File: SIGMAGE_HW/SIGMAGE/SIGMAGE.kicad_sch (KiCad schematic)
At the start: 0 parts

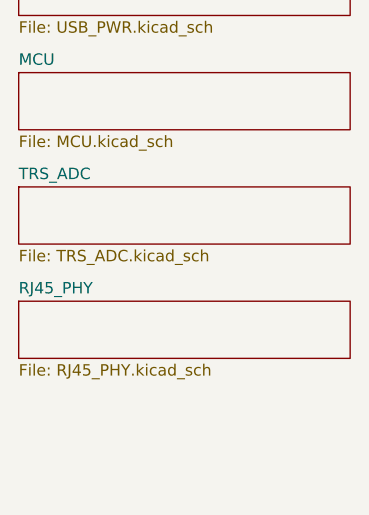
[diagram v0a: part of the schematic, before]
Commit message: Adding a view DAC's
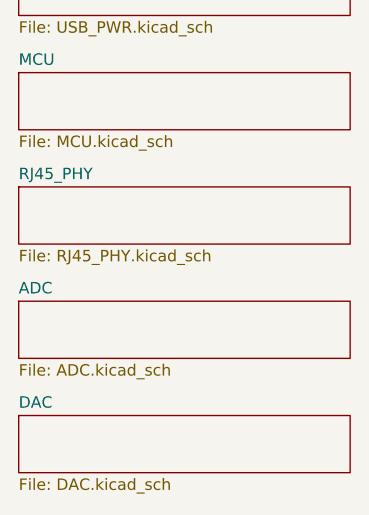
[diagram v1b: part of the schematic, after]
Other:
- removed sheet TRS_ADC
- added sheet ADC (ADC.kicad_sch)
- added sheet DAC (DAC.kicad_sch)
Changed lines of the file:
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@@
+	)
+	(sheet
+		(at 17.78 57.15)
+		(size 36.83 6.35)
+		(exclude_from_sim no)
+		(in_bom yes)
+		(on_board yes)
+		(dnp no)
+		(fields_autoplaced yes)
+		(stroke
+			(width 0.1524)
+			(type solid)
+		)
+		(fill
+			(color 0 0 0 0)
+		)
+		(property "Sheetname" "ADC"
+			(at 17.78 56.4384 0)
+			(show_name no)
+			(do_not_autoplace no)
+			(effects
+				(font
+					(size 1.27 1.27)
+				)
+				(justify left bottom)
+			)
+		)
+		(property "Sheetfile" "ADC.kicad_sch"
+			(at 17.78 64.0846 0)
+			(show_name no)
+			(do_not_autoplace no)
+			(effects
+				(font
+					(size 1.27 1.27)
+				)
+				(justify left top)
+			)
+		)
+		(instances
+			(project "SIGMAGE"
+				(path "/6fbe3371-b6a3-4e28-aef4-4e5865f4674e"
+					(page "3")
+				)
+			)
+		)
 	)
 	(sheet
@@
 			(color 0 0 0 0)
 		)
-		(property "Sheetname" "TRS_ADC"
+		(property "Sheetname" "RJ45_PHY"
 			(at 17.78 43.7384 0)
 			(show_name no)
@@
 			)
 		)
-		(property "Sheetfile" "TRS_ADC.kicad_sch"
+		(property "Sheetfile" "RJ45_PHY.kicad_sch"
 			(at 17.78 51.3846 0)
 			(show_name no)
@@
 	)
 	(sheet
-		(at 17.78 57.15)
+		(at 17.78 69.85)
 		(size 36.83 6.35)
 		(exclude_from_sim no)
@@
 			(color 0 0 0 0)
 		)
-		(property "Sheetname" "RJ45_PHY"
-			(at 17.78 56.4384 0)
+		(property "Sheetname" "DAC"
+			(at 17.78 69.1384 0)
 			(show_name no)
 			(do_not_autoplace no)
@@
 			)
 		)
-		(property "Sheetfile" "RJ45_PHY.kicad_sch"
-			(at 17.78 64.0846 0)
+		(property "Sheetfile" "DAC.kicad_sch"
+			(at 17.78 76.7846 0)
 			(show_name no)
 			(do_not_autoplace no)
@@
 			(project "SIGMAGE"
 				(path "/6fbe3371-b6a3-4e28-aef4-4e5865f4674e"
-					(page "5")
+					(page "6")
 				)
 			)

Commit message: some schematic adjustments
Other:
- removed sheet MCU
- removed sheet RJ45_PHY
- added sheet FPGA (FPGA.kicad_sch)
- added sheet PWR (PWR.kicad_sch)
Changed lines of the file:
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@@
 	(paper "A4")
 	(sheet
-		(at 17.78 31.75)
-		(size 36.83 6.35)
-		(exclude_from_sim no)
-		(in_bom yes)
-		(on_board yes)
-		(dnp no)
-		(fields_autoplaced yes)
-		(stroke
-			(width 0.1524)
-			(type solid)
-		)
-		(fill
-			(color 0 0 0 0)
-		)
-		(property "Sheetname" "MCU"
-			(at 17.78 31.0384 0)
-			(show_name no)
-			(do_not_autoplace no)
-			(effects
-				(font
-					(size 1.27 1.27)
-				)
-				(justify left bottom)
-			)
-		)
-		(property "Sheetfile" "MCU.kicad_sch"
-			(at 17.78 38.6846 0)
+		(at 62.23 19.05)
+		(size 36.83 6.35)
+		(exclude_from_sim no)
+		(in_bom yes)
+		(on_board yes)
+		(dnp no)
+		(fields_autoplaced yes)
+		(stroke
+			(width 0.1524)
+			(type solid)
+		)
+		(fill
+			(color 0 0 0 0)
+		)
+		(property "Sheetname" "USB_PWR"
+			(at 62.23 18.3384 0)
+			(show_name no)
+			(do_not_autoplace no)
+			(effects
+				(font
+					(size 1.27 1.27)
+				)
+				(justify left bottom)
+			)
+		)
+		(property "Sheetfile" "USB_PWR.kicad_sch"
+			(at 62.23 25.9846 0)
+			(show_name no)
+			(do_not_autoplace no)
+			(effects
+				(font
+					(size 1.27 1.27)
+				)
+				(justify left top)
+			)
+		)
+		(instances
+			(project "SIGMAGE"
+				(path "/6fbe3371-b6a3-4e28-aef4-4e5865f4674e"
+					(page "2")
+				)
+			)
+		)
+	)
+	(sheet
+		(at 19.05 31.75)
+		(size 36.83 6.35)
+		(exclude_from_sim no)
+		(in_bom yes)
+		(on_board yes)
+		(dnp no)
+		(fields_autoplaced yes)
+		(stroke
+			(width 0.1524)
+			(type solid)
+		)
+		(fill
+			(color 0 0 0 0)
+		)
+		(property "Sheetname" "FPGA"
+			(at 19.05 31.0384 0)
+			(show_name no)
+			(do_not_autoplace no)
+			(effects
+				(font
+					(size 1.27 1.27)
+				)
+				(justify left bottom)
+			)
+		)
+		(property "Sheetfile" "FPGA.kicad_sch"
+			(at 19.05 38.6846 0)
 			(show_name no)
 			(do_not_autoplace no)
@@
 	)
 	(sheet
-		(at 17.78 19.05)
-		(size 36.83 6.35)
-		(exclude_from_sim no)
-		(in_bom yes)
-		(on_board yes)
-		(dnp no)
-		(fields_autoplaced yes)
-		(stroke
-			(width 0.1524)
-			(type solid)
-		)
-		(fill
-			(color 0 0 0 0)
-		)
-		(property "Sheetname" "USB_PWR"
-			(at 17.78 18.3384 0)
-			(show_name no)
-			(do_not_autoplace no)
-			(effects
-				(font
-					(size 1.27 1.27)
-				)
-				(justify left bottom)
-			)
-		)
-		(property "Sheetfile" "USB_PWR.kicad_sch"
-			(at 17.78 25.9846 0)
-			(show_name no)
-			(do_not_autoplace no)
-			(effects
-				(font
-					(size 1.27 1.27)
-				)
-				(justify left top)
-			)
-		)
-		(instances
-			(project "SIGMAGE"
-				(path "/6fbe3371-b6a3-4e28-aef4-4e5865f4674e"
-					(page "2")
-				)
-			)
-		)
-	)
-	(sheet
-		(at 17.78 57.15)
+		(at 19.05 19.05)
+		(size 36.83 6.35)
+		(exclude_from_sim no)
+		(in_bom yes)
+		(on_board yes)
+		(dnp no)
+		(fields_autoplaced yes)
+		(stroke
+			(width 0.1524)
+			(type solid)
+		)
+		(fill
+			(color 0 0 0 0)
+		)
+		(property "Sheetname" "PWR"
+			(at 19.05 18.3384 0)
+			(show_name no)
+			(do_not_autoplace no)
+			(effects
+				(font
+					(size 1.27 1.27)
+				)
+				(justify left bottom)
+			)
+		)
+		(property "Sheetfile" "PWR.kicad_sch"
+			(at 19.05 25.9846 0)
+			(show_name no)
+			(do_not_autoplace no)
+			(effects
+				(font
+					(size 1.27 1.27)
+				)
+				(justify left top)
+			)
+		)
+		(instances
+			(project "SIGMAGE"
+				(path "/6fbe3371-b6a3-4e28-aef4-4e5865f4674e"
+					(page "5")
+				)
+			)
+		)
+	)
+	(sheet
+		(at 19.05 44.45)
 		(size 36.83 6.35)
 		(exclude_from_sim no)
@@
 		)
 		(property "Sheetname" "ADC"
-			(at 17.78 56.4384 0)
+			(at 19.05 43.7384 0)
 			(show_name no)
 			(do_not_autoplace no)
@@
 		)
 		(property "Sheetfile" "ADC.kicad_sch"
-			(at 17.78 64.0846 0)
+			(at 19.05 51.3846 0)
 			(show_name no)
 			(do_not_autoplace no)
@@
 	)
 	(sheet
-		(at 17.78 44.45)
-		(size 36.83 6.35)
-		(exclude_from_sim no)
-		(in_bom yes)
-		(on_board yes)
-		(dnp no)
-		(fields_autoplaced yes)
-		(stroke
-			(width 0.1524)
-			(type solid)
-		)
-		(fill
-			(color 0 0 0 0)
-		)
-		(property "Sheetname" "RJ45_PHY"
-			(at 17.78 43.7384 0)
-			(show_name no)
-			(do_not_autoplace no)
-			(effects
-				(font
-					(size 1.27 1.27)
-				)
-				(justify left bottom)
-			)
-		)
-		(property "Sheetfile" "RJ45_PHY.kicad_sch"
-			(at 17.78 51.3846 0)
-			(show_name no)
-			(do_not_autoplace no)
-			(effects
-				(font
-					(size 1.27 1.27)
-				)
-				(justify left top)
-			)
-		)
-		(instances
-			(project "SIGMAGE"
-				(path "/6fbe3371-b6a3-4e28-aef4-4e5865f4674e"
-					(page "5")
-				)
-			)
-		)
-	)
-	(sheet
-		(at 17.78 69.85)
+		(at 19.05 57.15)
 		(size 36.83 6.35)
 		(exclude_from_sim no)
@@
 		)
 		(property "Sheetname" "DAC"
-			(at 17.78 69.1384 0)
+			(at 19.05 56.4384 0)
 			(show_name no)
 			(do_not_autoplace no)
@@
 		)
 		(property "Sheetfile" "DAC.kicad_sch"
-			(at 17.78 76.7846 0)
-			(show_name no)
-			(do_not_autoplace no)
+			(at 19.05 64.0846 0)
+			(show_name no)
+			(do_not_autoplace no)

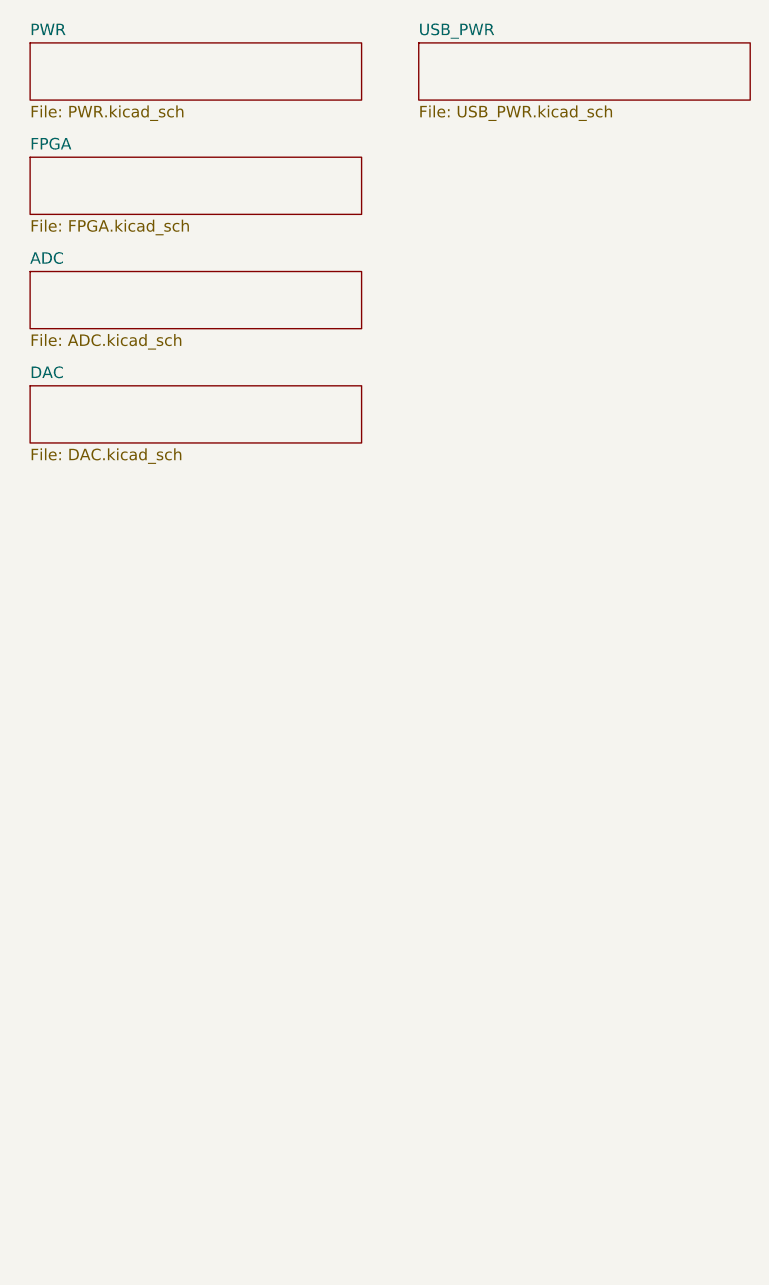
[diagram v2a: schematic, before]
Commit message: some USB interface
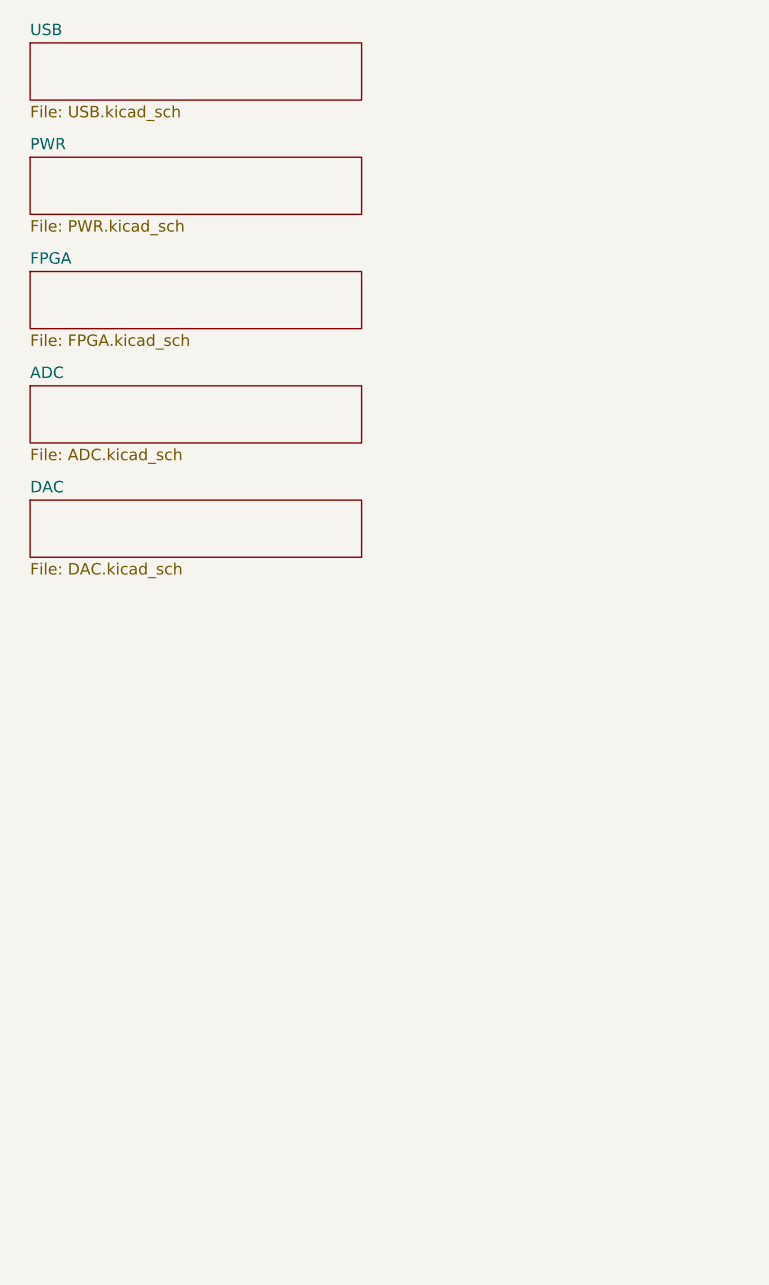
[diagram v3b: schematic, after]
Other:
- removed sheet USB_PWR
- added sheet USB (USB.kicad_sch)
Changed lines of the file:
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@@
 	(paper "A4")
 	(sheet
-		(at 62.23 19.05)
-		(size 36.83 6.35)
-		(exclude_from_sim no)
-		(in_bom yes)
-		(on_board yes)
-		(dnp no)
-		(fields_autoplaced yes)
-		(stroke
-			(width 0.1524)
-			(type solid)
-		)
-		(fill
-			(color 0 0 0 0)
-		)
-		(property "Sheetname" "USB_PWR"
-			(at 62.23 18.3384 0)
-			(show_name no)
-			(do_not_autoplace no)
-			(effects
-				(font
-					(size 1.27 1.27)
-				)
-				(justify left bottom)
-			)
-		)
-		(property "Sheetfile" "USB_PWR.kicad_sch"
-			(at 62.23 25.9846 0)
-			(show_name no)
-			(do_not_autoplace no)
-			(effects
-				(font
-					(size 1.27 1.27)
-				)
-				(justify left top)
-			)
-		)
-		(instances
-			(project "SIGMAGE"
-				(path "/6fbe3371-b6a3-4e28-aef4-4e5865f4674e"
-					(page "2")
+		(at 19.05 44.45)
+		(size 36.83 6.35)
+		(exclude_from_sim no)
+		(in_bom yes)
+		(on_board yes)
+		(dnp no)
+		(fields_autoplaced yes)
+		(stroke
+			(width 0.1524)
+			(type solid)
+		)
+		(fill
+			(color 0 0 0 0)
+		)
+		(property "Sheetname" "FPGA"
+			(at 19.05 43.7384 0)
+			(show_name no)
+			(do_not_autoplace no)
+			(effects
+				(font
+					(size 1.27 1.27)
+				)
+				(justify left bottom)
+			)
+		)
+		(property "Sheetfile" "FPGA.kicad_sch"
+			(at 19.05 51.3846 0)
+			(show_name no)
+			(do_not_autoplace no)
+			(effects
+				(font
+					(size 1.27 1.27)
+				)
+				(justify left top)
+			)
+		)
+		(instances
+			(project "SIGMAGE"
+				(path "/6fbe3371-b6a3-4e28-aef4-4e5865f4674e"
+					(page "4")
 				)
 			)
@@
 			(color 0 0 0 0)
 		)
-		(property "Sheetname" "FPGA"
+		(property "Sheetname" "PWR"
 			(at 19.05 31.0384 0)
 			(show_name no)
@@
 			)
 		)
-		(property "Sheetfile" "FPGA.kicad_sch"
+		(property "Sheetfile" "PWR.kicad_sch"
 			(at 19.05 38.6846 0)
 			(show_name no)
@@
 			(project "SIGMAGE"
 				(path "/6fbe3371-b6a3-4e28-aef4-4e5865f4674e"
-					(page "4")
+					(page "5")
+				)
+			)
+		)
+	)
+	(sheet
+		(at 19.05 57.15)
+		(size 36.83 6.35)
+		(exclude_from_sim no)
+		(in_bom yes)
+		(on_board yes)
+		(dnp no)
+		(fields_autoplaced yes)
+		(stroke
+			(width 0.1524)
+			(type solid)
+		)
+		(fill
+			(color 0 0 0 0)
+		)
+		(property "Sheetname" "ADC"
+			(at 19.05 56.4384 0)
+			(show_name no)
+			(do_not_autoplace no)
+			(effects
+				(font
+					(size 1.27 1.27)
+				)
+				(justify left bottom)
+			)
+		)
+		(property "Sheetfile" "ADC.kicad_sch"
+			(at 19.05 64.0846 0)
+			(show_name no)
+			(do_not_autoplace no)
+			(effects
+				(font
+					(size 1.27 1.27)
+				)
+				(justify left top)
+			)
+		)
+		(instances
+			(project "SIGMAGE"
+				(path "/6fbe3371-b6a3-4e28-aef4-4e5865f4674e"
+					(page "3")
 				)
 			)
@@
 			(color 0 0 0 0)
 		)
-		(property "Sheetname" "PWR"
+		(property "Sheetname" "USB"
 			(at 19.05 18.3384 0)
 			(show_name no)
@@
 			)
 		)
-		(property "Sheetfile" "PWR.kicad_sch"
+		(property "Sheetfile" "USB.kicad_sch"
 			(at 19.05 25.9846 0)
 			(show_name no)
@@
 			(project "SIGMAGE"
 				(path "/6fbe3371-b6a3-4e28-aef4-4e5865f4674e"
-					(page "5")
-				)
-			)
-		)
-	)
-	(sheet
-		(at 19.05 44.45)
-		(size 36.83 6.35)
-		(exclude_from_sim no)
-		(in_bom yes)
-		(on_board yes)
-		(dnp no)
-		(fields_autoplaced yes)
-		(stroke
-			(width 0.1524)
-			(type solid)
-		)
-		(fill
-			(color 0 0 0 0)
-		)
-		(property "Sheetname" "ADC"
-			(at 19.05 43.7384 0)
-			(show_name no)
-			(do_not_autoplace no)
-			(effects
-				(font
-					(size 1.27 1.27)
-				)
-				(justify left bottom)
-			)
-		)
-		(property "Sheetfile" "ADC.kicad_sch"
-			(at 19.05 51.3846 0)
-			(show_name no)
-			(do_not_autoplace no)
-			(effects
-				(font
-					(size 1.27 1.27)
-				)
-				(justify left top)
-			)
-		)
-		(instances
-			(project "SIGMAGE"
-				(path "/6fbe3371-b6a3-4e28-aef4-4e5865f4674e"
-					(page "3")
-				)
-			)
-		)
-	)
-	(sheet
-		(at 19.05 57.15)
+					(page "7")
+				)
+			)
+		)
+	)
+	(sheet
+		(at 19.05 69.85)
 		(size 36.83 6.35)
 		(exclude_from_sim no)
@@
 		)
 		(property "Sheetname" "DAC"
-			(at 19.05 56.4384 0)
+			(at 19.05 69.1384 0)
 			(show_name no)
 			(do_not_autoplace no)
@@
 		)
 		(property "Sheetfile" "DAC.kicad_sch"
-			(at 19.05 64.0846 0)
-			(show_name no)
-			(do_not_autoplace no)
+			(at 19.05 76.7846 0)
+			(show_name no)
+			(do_not_autoplace no)

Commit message: some changes
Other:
- added sheet ENC (ENC.kicad_sch)
- added sheet MCU (MCU.kicad_sch)
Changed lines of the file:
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@@
 	(paper "A4")
 	(sheet
-		(at 19.05 44.45)
+		(at 19.05 57.15)
 		(size 36.83 6.35)
 		(exclude_from_sim no)
@@
 		)
 		(property "Sheetname" "FPGA"
-			(at 19.05 43.7384 0)
+			(at 19.05 56.4384 0)
 			(show_name no)
 			(do_not_autoplace no)
@@
 		)
 		(property "Sheetfile" "FPGA.kicad_sch"
-			(at 19.05 51.3846 0)
+			(at 19.05 64.0846 0)
 			(show_name no)
 			(do_not_autoplace no)
@@
 	)
 	(sheet
-		(at 19.05 57.15)
+		(at 19.05 44.45)
+		(size 36.83 6.35)
+		(exclude_from_sim no)
+		(in_bom yes)
+		(on_board yes)
+		(dnp no)
+		(fields_autoplaced yes)
+		(stroke
+			(width 0.1524)
+			(type solid)
+		)
+		(fill
+			(color 0 0 0 0)
+		)
+		(property "Sheetname" "MCU"
+			(at 19.05 43.7384 0)
+			(show_name no)
+			(do_not_autoplace no)
+			(effects
+				(font
+					(size 1.27 1.27)
+				)
+				(justify left bottom)
+			)
+		)
+		(property "Sheetfile" "MCU.kicad_sch"
+			(at 19.05 51.3846 0)
+			(show_name no)
+			(do_not_autoplace no)
+			(effects
+				(font
+					(size 1.27 1.27)
+				)
+				(justify left top)
+			)
+		)
+		(instances
+			(project "SIGMAGE"
+				(path "/6fbe3371-b6a3-4e28-aef4-4e5865f4674e"
+					(page "2")
+				)
+			)
+		)
+	)
+	(sheet
+		(at 19.05 69.85)
 		(size 36.83 6.35)
 		(exclude_from_sim no)
@@
 		)
 		(property "Sheetname" "ADC"
-			(at 19.05 56.4384 0)
+			(at 19.05 69.1384 0)
 			(show_name no)
 			(do_not_autoplace no)
@@
 		)
 		(property "Sheetfile" "ADC.kicad_sch"
-			(at 19.05 64.0846 0)
+			(at 19.05 76.7846 0)
 			(show_name no)
 			(do_not_autoplace no)
@@
 	)
 	(sheet
-		(at 19.05 69.85)
+		(at 19.05 82.55)
 		(size 36.83 6.35)
 		(exclude_from_sim no)
@@
 		)
 		(property "Sheetname" "DAC"
-			(at 19.05 69.1384 0)
+			(at 19.05 81.8384 0)
 			(show_name no)
 			(do_not_autoplace no)
@@
 		)
 		(property "Sheetfile" "DAC.kicad_sch"
-			(at 19.05 76.7846 0)
+			(at 19.05 89.4846 0)
 			(show_name no)
 			(do_not_autoplace no)
@@
 				)
 			)
+		)
+	)
+	(sheet
+		(at 19.05 95.25)
+		(size 36.83 6.35)
+		(exclude_from_sim no)
+		(in_bom yes)
+		(on_board yes)
+		(dnp no)
+		(fields_autoplaced yes)
+		(stroke
+			(width 0.1524)
+			(type solid)
+		)
+		(fill
+			(color 0 0 0 0)
+		)
+		(property "Sheetname" "ENC"
+			(at 19.05 94.5384 0)
+			(show_name no)
+			(do_not_autoplace no)
+			(effects
+				(font
+					(size 1.27 1.27)
+				)
+				(justify left bottom)
+			)
+		)
+		(property "Sheetfile" "ENC.kicad_sch"
+			(at 19.05 102.1846 0)
+			(show_name no)
+			(do_not_autoplace no)
+			(effects
+				(font
+					(size 1.27 1.27)
+				)
+				(justify left top)
+			)
+		)
+		(instances
+			(project "SIGMAGE"
+				(path "/6fbe3371-b6a3-4e28-aef4-4e5865f4674e"
+					(page "8")
+				)
+			)

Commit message: major changes
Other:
- added sheet BTN (BTN.kicad_sch)
- added sheet LED (LED.kicad_sch)
- added sheet SDCARD (SDCARD.kicad_sch)
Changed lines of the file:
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@@
 	(paper "A4")
+	(sheet
+		(at 19.05 120.65)
+		(size 36.83 6.35)
+		(exclude_from_sim no)
+		(in_bom yes)
+		(on_board yes)
+		(dnp no)
+		(fields_autoplaced yes)
+		(stroke
+			(width 0.1524)
+			(type solid)
+		)
+		(fill
+			(color 0 0 0 0)
+		)
+		(property "Sheetname" "BTN"
+			(at 19.05 119.9384 0)
+			(show_name no)
+			(do_not_autoplace no)
+			(effects
+				(font
+					(size 1.27 1.27)
+				)
+				(justify left bottom)
+			)
+		)
+		(property "Sheetfile" "BTN.kicad_sch"
+			(at 19.05 127.5846 0)
+			(show_name no)
+			(do_not_autoplace no)
+			(effects
+				(font
+					(size 1.27 1.27)
+				)
+				(justify left top)
+			)
+		)
+		(instances
+			(project "SIGMAGE"
+				(path "/6fbe3371-b6a3-4e28-aef4-4e5865f4674e"
+					(page "10")
+				)
+			)
+		)
+	)
 	(sheet
 		(at 19.05 57.15)
@@
 				)
 			)
+		)
+	)
+	(sheet
+		(at 19.05 107.95)
+		(size 36.83 6.35)
+		(exclude_from_sim no)
+		(in_bom yes)
+		(on_board yes)
+		(dnp no)
+		(fields_autoplaced yes)
+		(stroke
+			(width 0.1524)
+			(type solid)
+		)
+		(fill
+			(color 0 0 0 0)
+		)
+		(property "Sheetname" "LED"
+			(at 19.05 107.2384 0)
+			(show_name no)
+			(do_not_autoplace no)
+			(effects
+				(font
+					(size 1.27 1.27)
+				)
+				(justify left bottom)
+			)
+		)
+		(property "Sheetfile" "LED.kicad_sch"
+			(at 19.05 114.8846 0)
+			(show_name no)
+			(do_not_autoplace no)
+			(effects
+				(font
+					(size 1.27 1.27)
+				)
+				(justify left top)
+			)
+		)
+		(instances
+			(project "SIGMAGE"
+				(path "/6fbe3371-b6a3-4e28-aef4-4e5865f4674e"
+					(page "9")
+				)
+			)
+		)
+	)
+	(sheet
+		(at 19.05 133.35)
+		(size 36.83 6.35)
+		(exclude_from_sim no)
+		(in_bom yes)
+		(on_board yes)
+		(dnp no)
+		(fields_autoplaced yes)
+		(stroke
+			(width 0.1524)
+			(type solid)
+		)
+		(fill
+			(color 0 0 0 0)
+		)
+		(property "Sheetname" "SDCARD"
+			(at 19.05 132.6384 0)
+			(show_name no)
+			(do_not_autoplace no)
+			(effects
+				(font
+					(size 1.27 1.27)
+				)
+				(justify left bottom)
+			)
+		)
+		(property "Sheetfile" "SDCARD.kicad_sch"
+			(at 19.05 140.2846 0)
+			(show_name no)
+			(do_not_autoplace no)
+			(effects
+				(font
+					(size 1.27 1.27)
+				)
+				(justify left top)
+			)
+		)
+		(instances
+			(project "SIGMAGE"
+				(path "/6fbe3371-b6a3-4e28-aef4-4e5865f4674e"
+					(page "11")
+				)
+			)

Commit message: before sync sheets
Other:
- added sheet MEZZ (MEZZ.kicad_sch)
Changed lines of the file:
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@@
+	)
+	(sheet
+		(at 19.05 146.05)
+		(size 36.83 6.35)
+		(exclude_from_sim no)
+		(in_bom yes)
+		(on_board yes)
+		(dnp no)
+		(fields_autoplaced yes)
+		(stroke
+			(width 0.1524)
+			(type solid)
+		)
+		(fill
+			(color 0 0 0 0)
+		)
+		(property "Sheetname" "MEZZ"
+			(at 19.05 145.3384 0)
+			(show_name no)
+			(do_not_autoplace no)
+			(effects
+				(font
+					(size 1.27 1.27)
+				)
+				(justify left bottom)
+			)
+		)
+		(property "Sheetfile" "MEZZ.kicad_sch"
+			(at 19.05 152.9846 0)
+			(show_name no)
+			(do_not_autoplace no)
+			(effects
+				(font
+					(size 1.27 1.27)
+				)
+				(justify left top)
+			)
+		)
+		(instances
+			(project "SIGMAGE"
+				(path "/6fbe3371-b6a3-4e28-aef4-4e5865f4674e"
+					(page "12")
+				)
+			)
+		)
 	)
 	(sheet
